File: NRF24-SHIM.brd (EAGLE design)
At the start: 27.9 x 50.8 mm, 21 parts

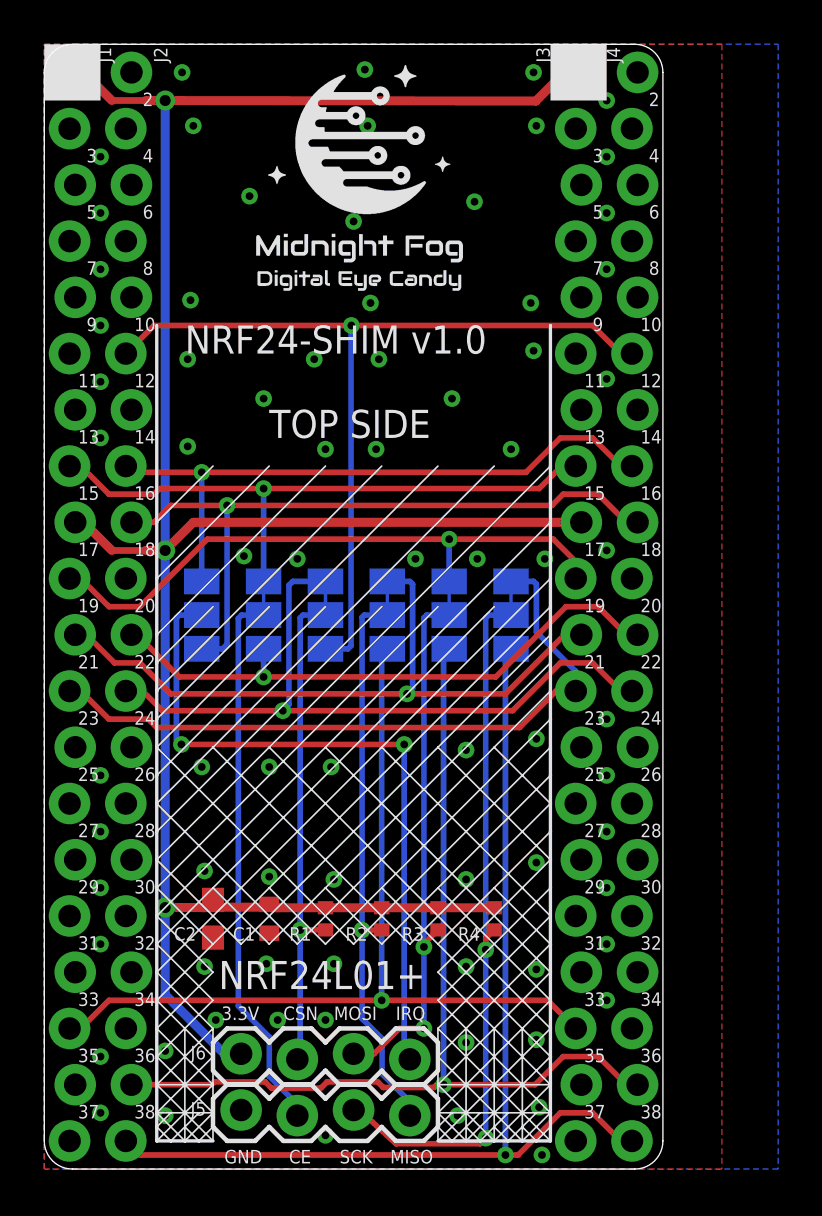
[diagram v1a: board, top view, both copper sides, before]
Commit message: Use more locking pin headers. Moved some traces.
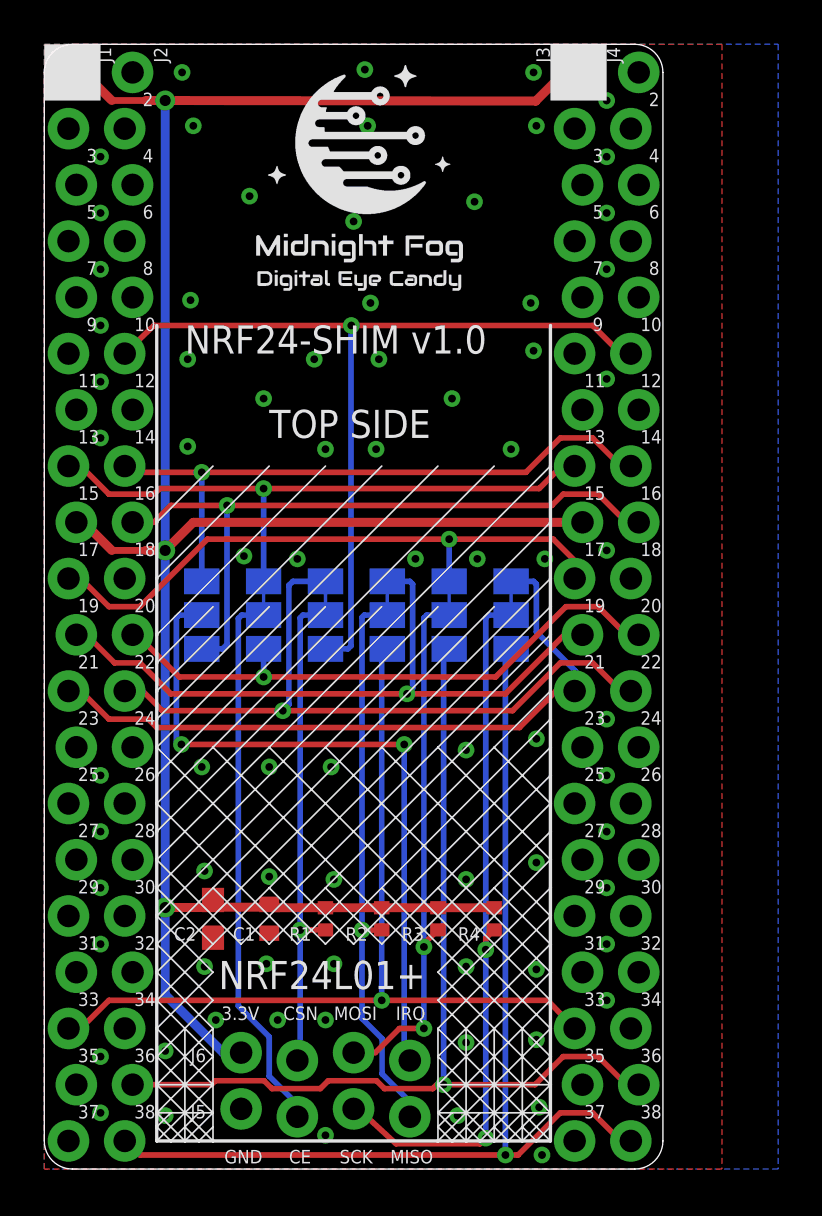
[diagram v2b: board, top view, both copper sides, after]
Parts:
- J1, J2, J3, J4: device SparkFun-Connectors:1X20_LOCK_NOSILK -> _my_locked_connectors:1X20_LOCK
- J5, J6: device SparkFun-Connectors:1X04_LOCK -> _my_locked_connectors:1X04_LOCK

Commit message: Made minor adjustments to traces and vias.
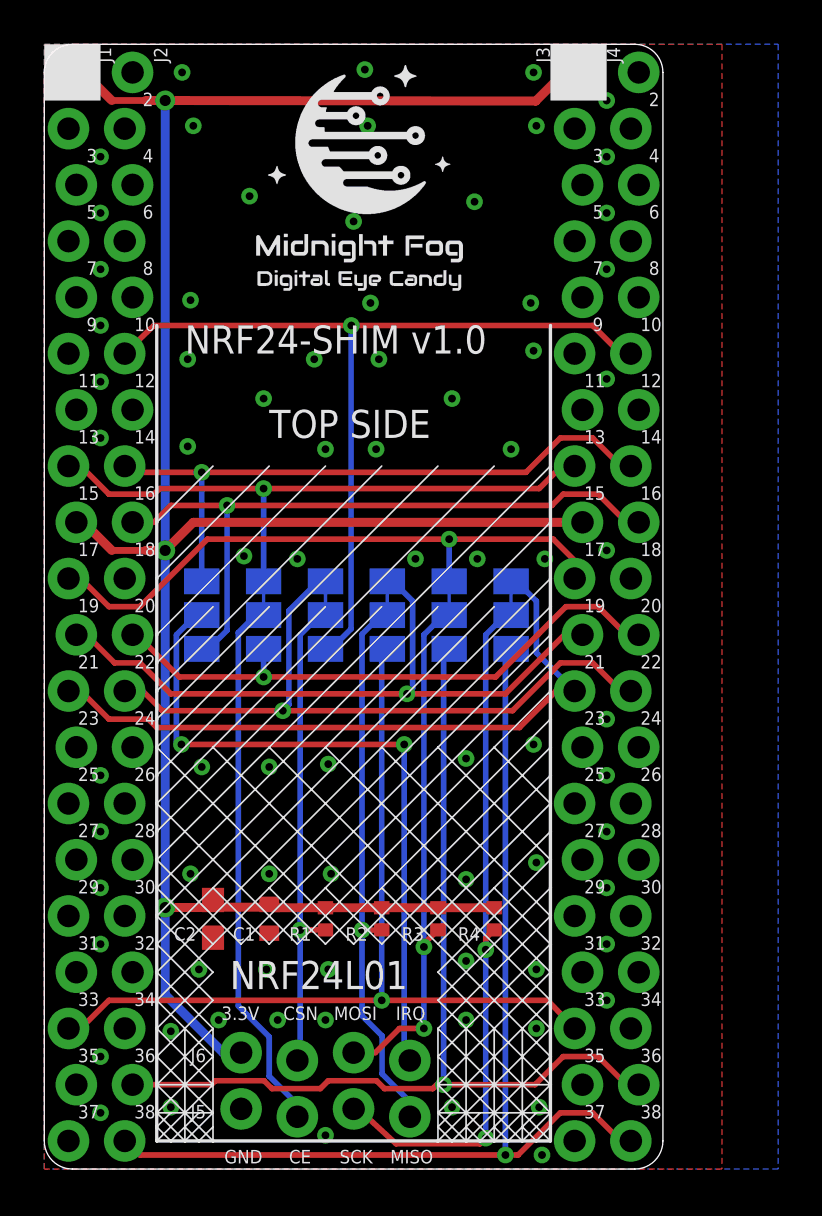
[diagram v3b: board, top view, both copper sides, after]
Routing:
- net CSN0: track 32.2 -> 31.5 mm
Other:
- board text added: "NRF24L01"
- board text removed: "NRF24L01+"
